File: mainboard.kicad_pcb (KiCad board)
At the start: 2 copper layers, 64.8 x 61.1 mm, 46 parts, among them J1 Screw_Terminal_1x02, SW1 SW_Push, SW2 SW_Push, U1 AT90CAN128-16MU, U2 MCP2551-I/SN, Y1 Crystal

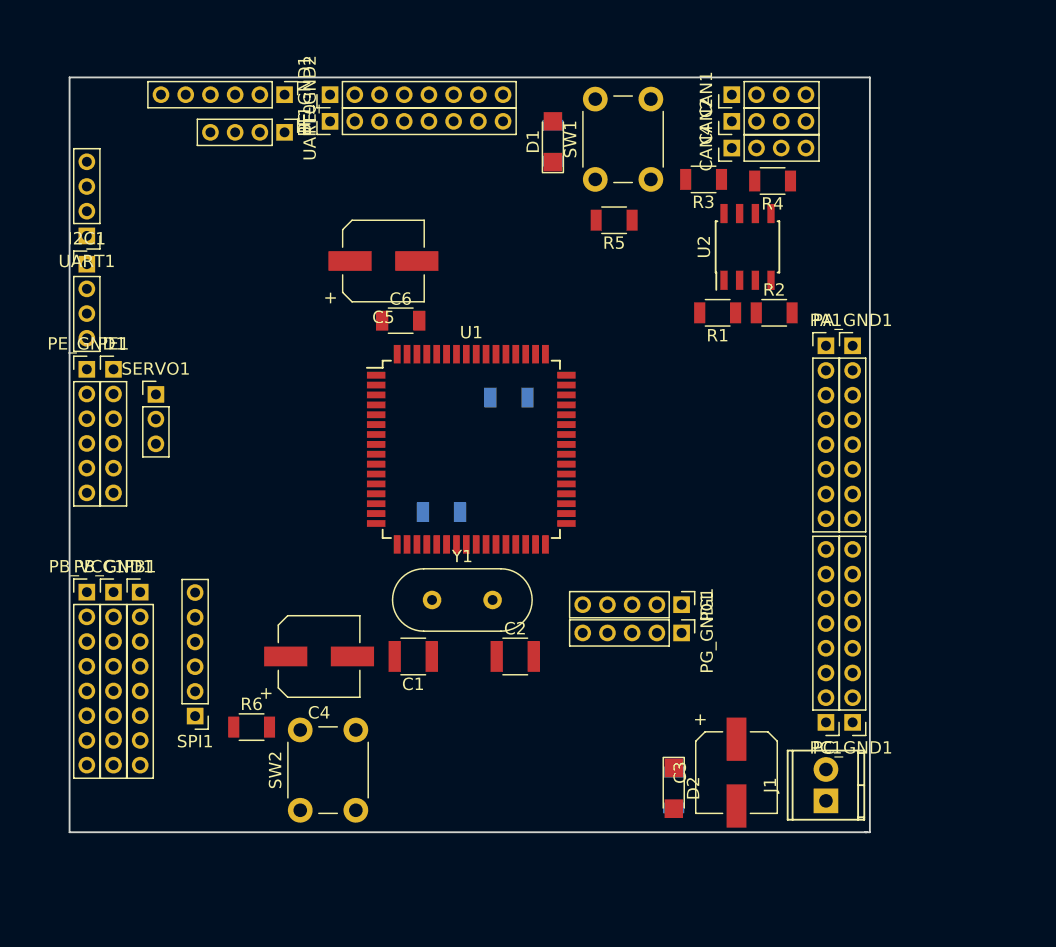
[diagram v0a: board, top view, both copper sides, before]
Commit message: Added protection, made board design and routing
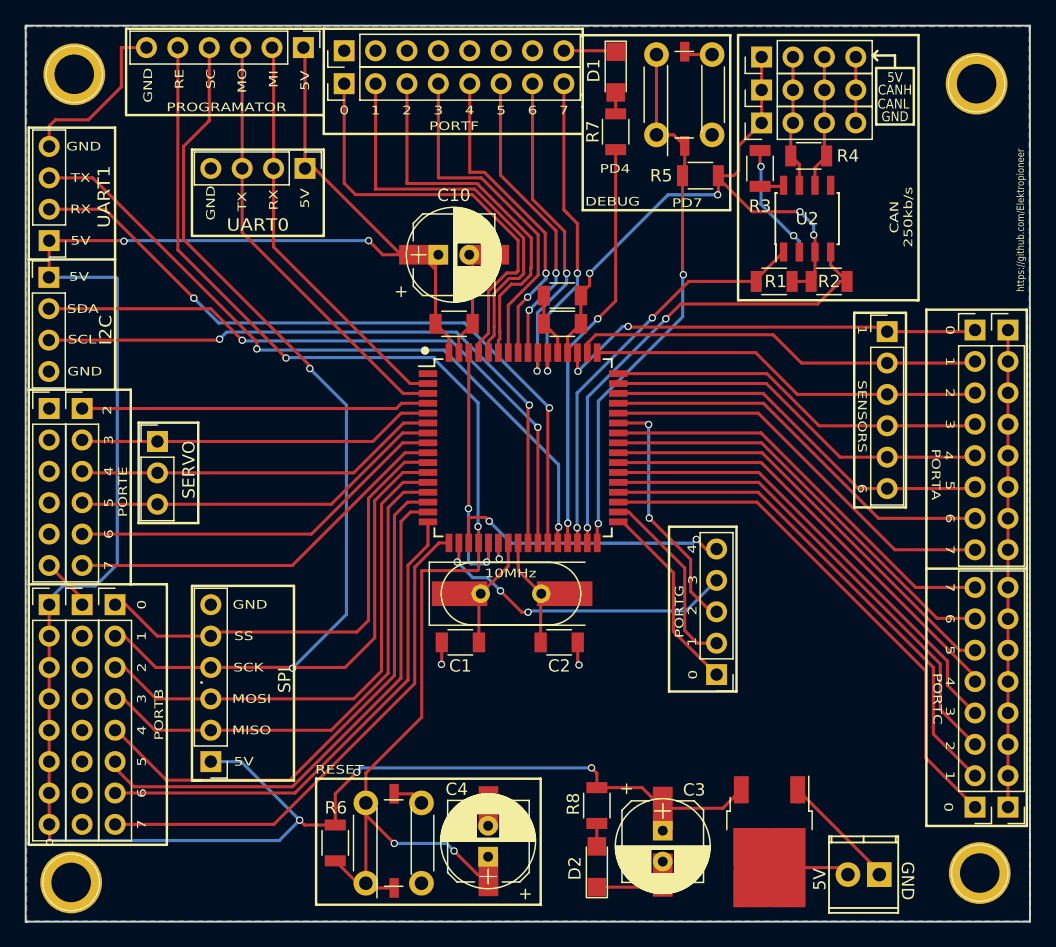
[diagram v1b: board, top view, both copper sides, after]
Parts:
- removed PG_GND1: CONN_01X05, Pin_Headers:Pin_Header_Straight_1x05_Pitch2.00mm
- removed SERVO1: CONN_01X03, Pin_Headers:Pin_Header_Straight_1x03_Pitch2.00mm
- removed SPI1: CONN_01X06, Pin_Headers:Pin_Header_Straight_1x06_Pitch2.00mm
- added C10: 100u, Capacitors_THT:CP_Radial_D7.5mm_P2.50mm, F.Cu at (95.5, 55.5)
- added C11: 100u, Capacitors_THT:CP_Radial_D7.5mm_P2.50mm, F.Cu at (99.5, 104.2)
- added C9: 100u, Capacitors_THT:CP_Radial_D7.5mm_P2.50mm, F.Cu at (113.7, 102.1)
- added Q1: IRF9540N, TO_SOT_Packages_SMD:TO-252-2, F.Cu at (122.3, 103.0)
- added REF**: 1pin, Connectors:1pin, F.Cu at (66.0, 40.9)
- added REF**: 1pin, Connectors:1pin, F.Cu at (65.8, 106.3)
- added REF**: 1pin, Connectors:1pin, F.Cu at (139.1, 41.7)
- added REF**: 1pin, Connectors:1pin, F.Cu at (139.3, 105.5)
- added SENSOR1: CONN_01X06, Pin_Headers:Pin_Header_Straight_1x06_Pitch2.54mm, F.Cu at (131.8, 61.7)
- added SERVO: CONN_01X03, Pin_Headers:Pin_Header_Straight_1x03_Pitch2.54mm, F.Cu at (72.8, 70.6)
- added SPI: CONN_01X06, Pin_Headers:Pin_Header_Straight_1x06_Pitch2.54mm, F.Cu at (77.1, 96.5)
- added SW_SMD1: RESET_SW, Buttons_Switches_SMD:SW_DIP_x1_W7.62mm_Slide_Copal_CHS-B, F.Cu at (91.9, 102.9)
- added SW_SMD2: DEBUG_SW, Buttons_Switches_SMD:SW_DIP_x1_W7.62mm_Slide_Copal_CHS-B, F.Cu at (115.4, 42.9)
- added Y_SMD1: Crystal, Crystals:Crystal_SMD_HC49-SD, F.Cu at (101.5, 82.9)
- C1, C2: footprint Capacitors_SMD:C_1210 -> Capacitors_SMD:C_1206
- C7, C8, R7, R8: moved to F.Cu
- CAN1, CAN2, CAN4, I2C1, UART0, UART1: footprint Pin_Headers:Pin_Header_Straight_1x04_Pitch2.00mm -> Pin_Headers:Pin_Header_Straight_1x04_Pitch2.54mm
- PA1, PA_GND1, PB1, PB_GND1, PB_VCC1, PC1, PC_GND1, PF1, PF_GND1: footprint Pin_Headers:Pin_Header_Straight_1x08_Pitch2.00mm -> Pin_Headers:Pin_Header_Straight_1x08_Pitch2.54mm
- PE1, PE_GND1, PE_GND2: footprint Pin_Headers:Pin_Header_Straight_1x06_Pitch2.00mm -> Pin_Headers:Pin_Header_Straight_1x06_Pitch2.54mm
- PG1: footprint Pin_Headers:Pin_Header_Straight_1x05_Pitch2.00mm -> Pin_Headers:Pin_Header_Straight_1x05_Pitch2.54mm
- SW_TH1: renamed from SW2; value SW_Push -> RESET_SW
- SW_TH2: renamed from SW1; value SW_Push -> DEBUG_SW
- moved C4 20.3 mm to (99.6, 103.0), turned to 90 degrees
- moved C8 20.1 mm to (105.5, 58.8), turned to 180 degrees
- moved PC_GND1 14.3 mm to (141.6, 100.2)
- moved PC1 13.9 mm to (138.9, 100.2)
- moved PA_GND1 12.6 mm to (141.6, 61.6)
- moved PA1 12.1 mm to (138.9, 61.6)
- moved R6 11.6 mm to (87.2, 103.1), turned to 270 degrees
- moved D2 8.89 mm to (108.3, 105.0), turned to 90 degrees
- moved C3 8.18 mm to (113.7, 103.0)
- moved SW_TH1 7.94 mm to (89.6, 106.4)
- moved R5 7.86 mm to (116.7, 49.1)
- moved D1 7.59 mm to (109.9, 40.7), turned to 270 degrees
- moved J1 7.37 mm to (131.2, 105.7), turned to 180 degrees
- moved C7 7.37 mm to (105.5, 61.1)
- moved R8 6.35 mm to (108.3, 100.1)
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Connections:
- J1 pad 2: +5V -> Net-(J1-Pad2)
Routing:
- net +5V: track 0.00 -> 263.8 mm, vias 0 -> 13
- net GND: track 0.00 -> 117.9 mm, vias 0 -> 6
- net RESET: track 0.00 -> 109.8 mm, vias 0 -> 4
- net PB1: track 0.00 -> 104.4 mm, vias 0 -> 2
- net RXD1: track 0.00 -> 58.1 mm, vias 0 -> 2
- net TXD1: track 0.00 -> 57.5 mm, vias 0 -> 2
- net SDA: track 0.00 -> 52.9 mm, vias 0 -> 2
- net SCL: track 0.00 -> 52.8 mm, vias 0 -> 2
- net PD7: track 0.00 -> 44.3 mm, vias 0 -> 2
- net PB4: track 0.00 -> 43.9 mm
- net PC0: track 0.00 -> 43.2 mm
- net PB5: track 0.00 -> 43.1 mm
- net PB3: track 0.00 -> 42.2 mm
- net PB7: track 0.00 -> 42.0 mm
- net PB2: track 0.00 -> 41.5 mm
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- added copper zone on B.Cu, net GND
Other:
- board size 64.8 x 61.1 mm -> 81.3 x 72.5 mm
- board text added: "0"
- board text added: "1"
- board text added: "10MHz"
- board text added: "2"
- board text added: "3"
- board text added: "4"
- board text added: "5"
- board text added: "5V"
- board text added: "6"
- board text added: "7"
- board text added: "CAN 250kb/s"
- board text added: "CANH"
- board text added: "CANL"
- board text added: "DEBUG"
- board text added: "GND"
- board text added: "I2C"
- board text added: "MI"
- board text added: "MISO"
- board text added: "MO"
- board text added: "MOSI"
- board text added: "PD4"
- board text added: "PD7"
- board text added: "PORTA"
- board text added: "PORTB"
- board text added: "PORTC"
- board text added: "PORTE"
- board text added: "PORTF"
- board text added: "PORTG"
- board text added: "PROGRAMATOR"
- board text added: "RE"
- board text added: "RESET"
- board text added: "RX"
- board text added: "SC"
- board text added: "SCK"
- board text added: "SCL"
- board text added: "SDA"
- board text added: "SENSORS"
- board text added: "SS"
- board text added: "TX"
- board text added: "UART0"
- board text added: "UART1"
- board text added: "https://github.com/Elektropioneer"

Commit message: Removed some trases
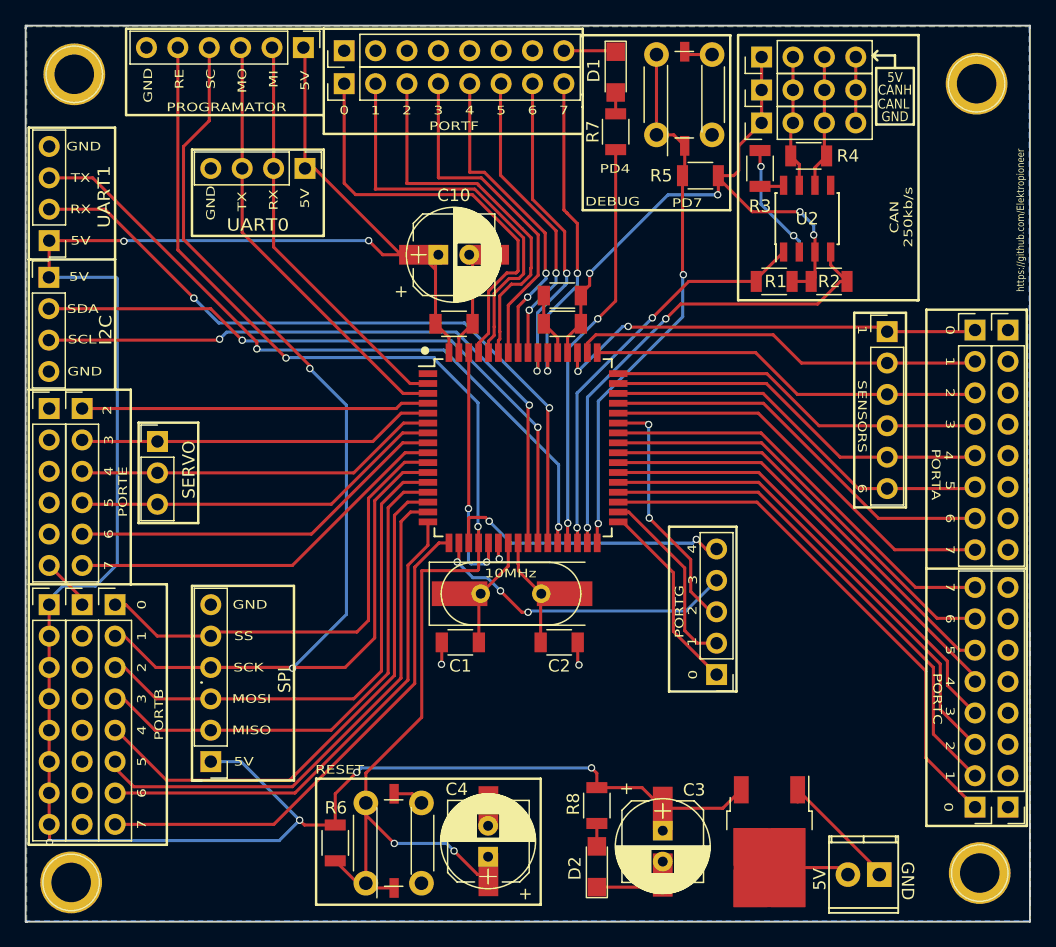
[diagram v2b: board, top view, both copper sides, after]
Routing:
- net GND: track 117.9 -> 65.2 mm
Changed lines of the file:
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@@
     (thickness 1.6)
     (drawings 182)
-    (tracks 630)
+    (tracks 609)
     (zones 0)
     (modules 57)
@@
   (segment (start 105.162 63.42) (end 105.162 62.212) (width 0.25) (layer F.Cu) (net 2))
   (segment (start 105.162 62.212) (end 104.037 61.087) (width 0.25) (layer F.Cu) (net 2))
-  (segment (start 141.605 100.203) (end 141.605 97.663) (width 0.25) (layer F.Cu) (net 2))
-  (segment (start 141.605 97.663) (end 141.605 95.123) (width 0.25) (layer F.Cu) (net 2))
-  (segment (start 141.605 95.123) (end 141.605 92.583) (width 0.25) (layer F.Cu) (net 2))
-  (segment (start 141.605 92.583) (end 141.605 90.043) (width 0.25) (layer F.Cu) (net 2))
-  (segment (start 141.605 90.043) (end 141.605 87.503) (width 0.25) (layer F.Cu) (net 2))
-  (segment (start 141.605 87.503) (end 141.605 84.963) (width 0.25) (layer F.Cu) (net 2))
-  (segment (start 141.605 84.963) (end 141.605 82.423) (width 0.25) (layer F.Cu) (net 2))
-  (segment (start 141.605 82.423) (end 141.605 79.375) (width 0.25) (layer F.Cu) (net 2))
-  (segment (start 141.605 79.375) (end 141.605 76.835) (width 0.25) (layer F.Cu) (net 2))
-  (segment (start 141.605 76.835) (end 141.605 74.295) (width 0.25) (layer F.Cu) (net 2))
-  (segment (start 141.605 74.295) (end 141.605 71.755) (width 0.25) (layer F.Cu) (net 2))
-  (segment (start 141.605 71.755) (end 141.605 69.215) (width 0.25) (layer F.Cu) (net 2))
-  (segment (start 141.605 69.215) (end 141.605 66.675) (width 0.25) (layer F.Cu) (net 2))
-  (segment (start 141.605 66.675) (end 141.605 64.135) (width 0.25) (layer F.Cu) (net 2))
-  (segment (start 141.605 64.135) (end 141.605 61.595) (width 0.25) (layer F.Cu) (net 2))
-  (segment (start 64.008 46.736) (end 64.008 45.085) (width 0.25) (layer F.Cu) (net 2))
-  (segment (start 64.008 45.085) (end 64.516 44.577) (width 0.25) (layer F.Cu) (net 2))
-  (segment (start 64.516 44.577) (end 67.183 44.577) (width 0.25) (layer F.Cu) (net 2))
-  (segment (start 67.183 44.577) (end 69.85 41.91) (width 0.25) (layer F.Cu) (net 2))
-  (segment (start 69.85 41.91) (end 69.85 38.735) (width 0.25) (layer F.Cu) (net 2))
-  (segment (start 69.85 38.735) (end 71.882 38.735) (width 0.25) (layer F.Cu) (net 2))
   (segment (start 129.286 39.497) (end 129.286 39.116) (width 0.25) (layer F.Cu) (net 2))
   (segment (start 115.443 39.0652) (end 115.3922 39.0652) (width 0.25) (layer F.Cu) (net 2))

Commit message: Removed some trases v2
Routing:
- net GND: track 65.2 -> 80.3 mm, vias 6 -> 7
- net +5V: track 263.8 -> 268.2 mm
- net Net-(C1-Pad1): track 9.03 -> 13.0 mm
- net Net-(C2-Pad1): track 8.84 -> 12.8 mm
- net CANL: track 10.8 -> 13.5 mm
- net Net-(J1-Pad2): track 6.58 -> 7.39 mm
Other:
- net class Default: trace_width 0.25 -> 0.5
